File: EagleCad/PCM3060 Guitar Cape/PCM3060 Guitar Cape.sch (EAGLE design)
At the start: 50 parts, among them J1 MONOSW, J2 MONOSW, U2 PCM3060_PW_28, U3 LM386

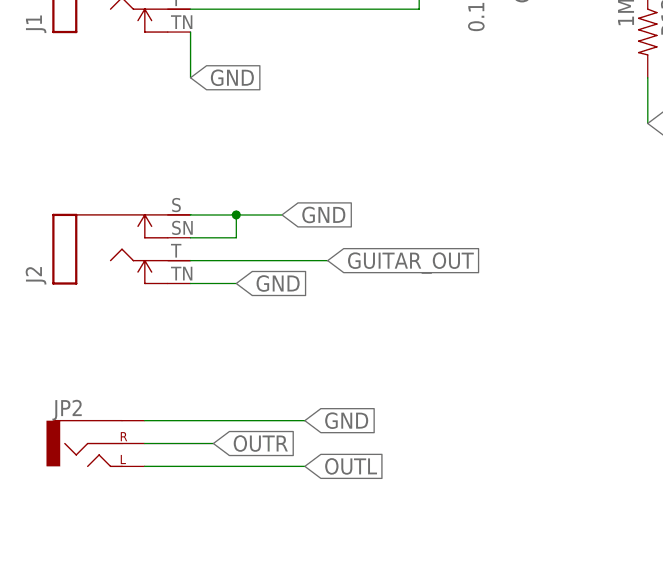
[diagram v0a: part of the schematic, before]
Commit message: Fixed Grounding Issue on Output Jack
Previously, the switched 1/4" output jack for the system would be
grounded when no cable was connected. This is correct for the input,
however grounding the output of the system is not proper.
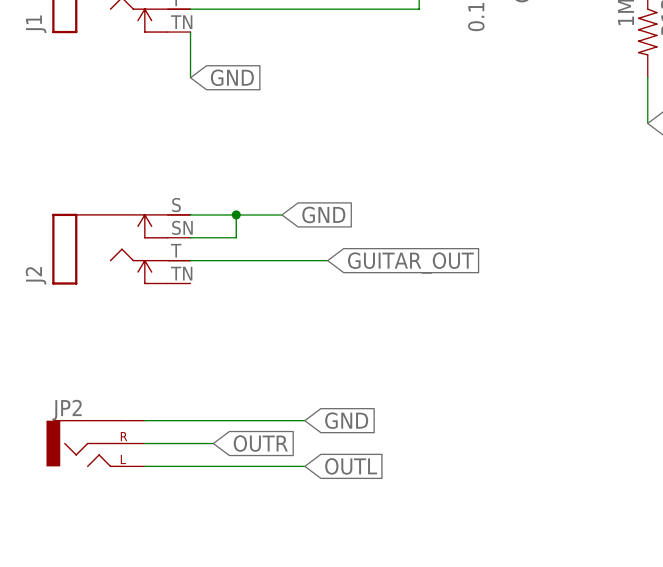
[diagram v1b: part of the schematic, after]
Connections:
- net GND: no longer J2.TN
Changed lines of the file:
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@@
-</segment>
-<segment>
-<pinref part="J2" gate="G$1" pin="TN"/>
-<wire x1="-96.52" y1="-157.48" x2="-91.44" y2="-157.48" width="0.1524" layer="91"/>
-<label x="-91.44" y="-157.48" size="1.778" layer="95" xref="yes"/>
 </segment>
 <segment>
